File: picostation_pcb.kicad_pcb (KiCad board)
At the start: 2 copper layers, 54.5 x 83.1 mm, 70 parts, among them J1 USB_C_Receptacle_USB2.0, J2 +, J3 D, J4 C, J5 G, J6 Conn_01x20, SW1 BOOT, U1 LM78M05_TO252, U3 RP2040, U4 W25Q16JVSSIQ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

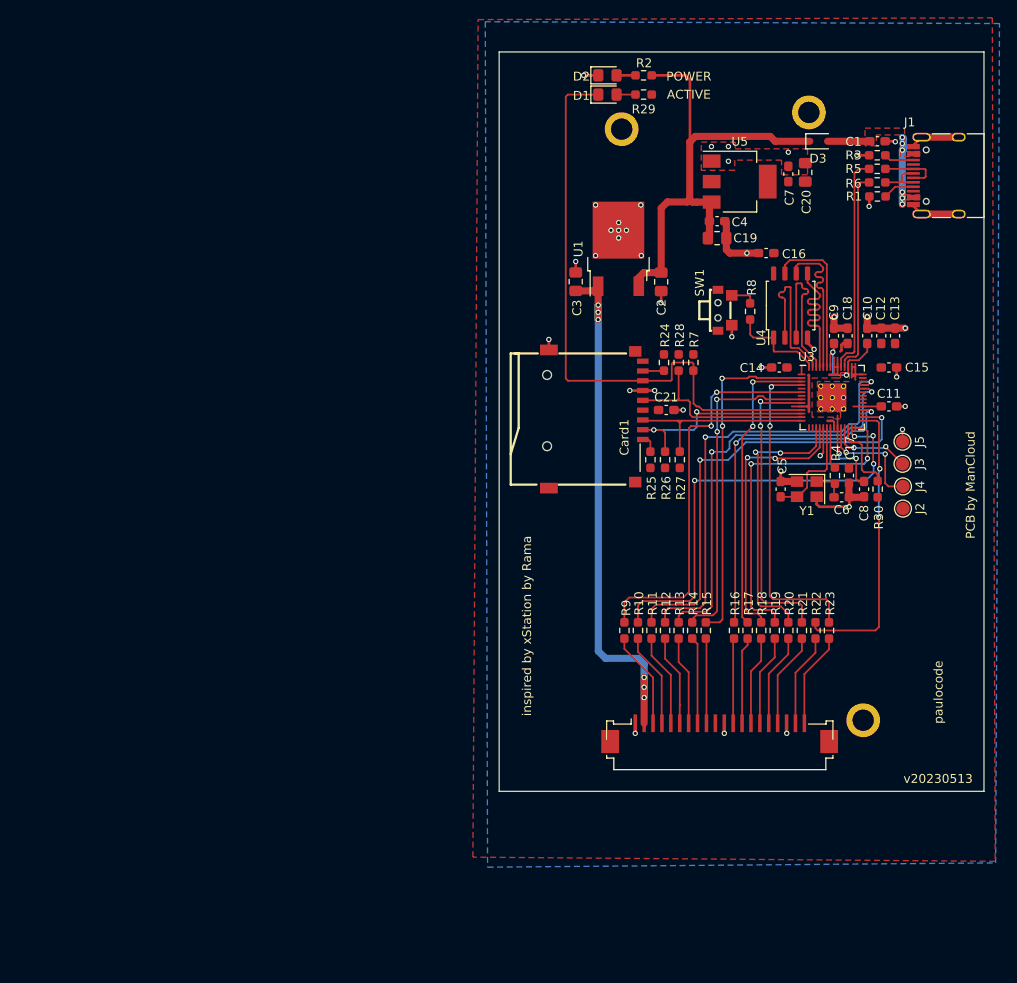
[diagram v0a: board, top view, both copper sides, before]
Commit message: Small PCB Improvements
Ordered a fully assembled board from JLCPCB, tested it for 5+ hours
while playing the fan translation of Policenauts. Tested several
other games as well for a short period of time (Silent Hill, Crash
Bandicoot, Spyro)

- Remove 5V 7805 regulator, diode OR the power from the 8V line into the
  AMS1117-3v3 instead (this part can accept up to 18V)
- Add a debug header that is compatible with the Raspberry Pi Debug
  Probe
- Add a reset switch
- Update photos
- Replace 2.2k resistors with 1k to improve ease of manufacturing
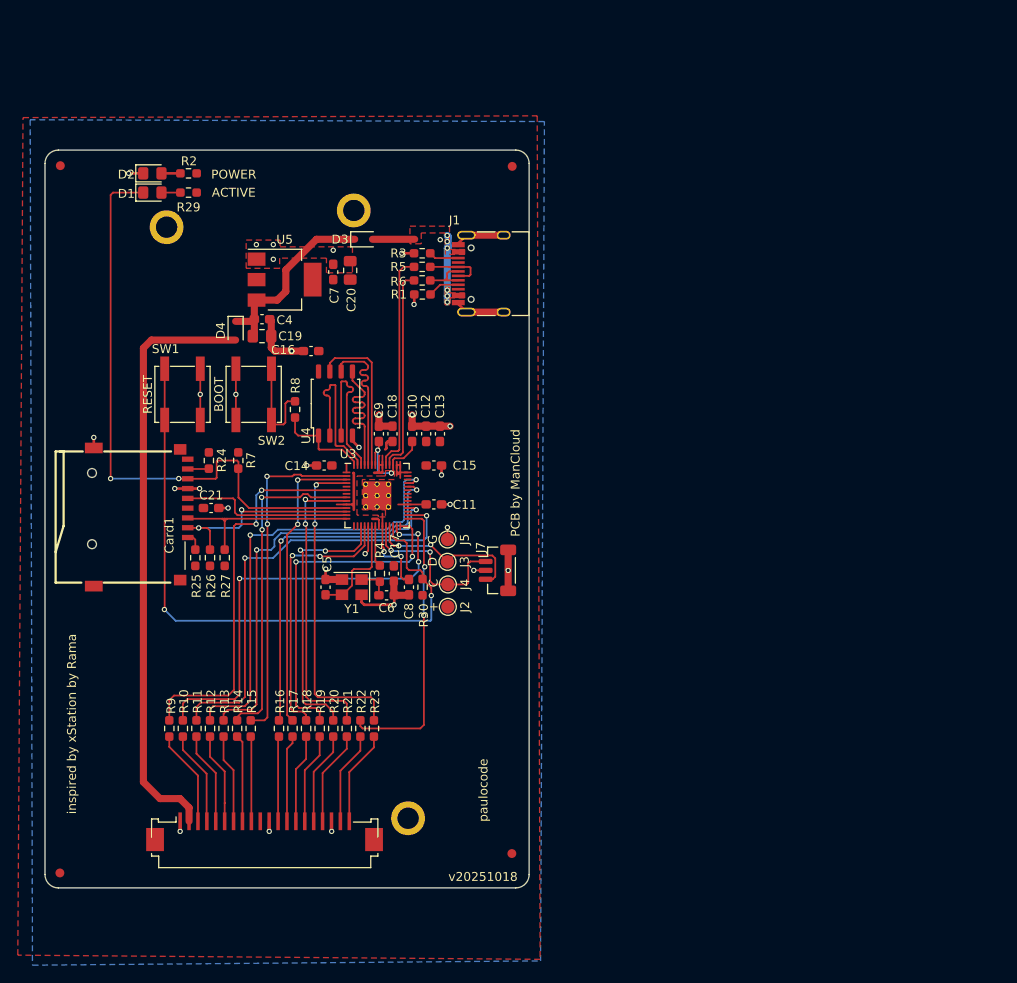
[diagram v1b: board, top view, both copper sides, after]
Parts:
- removed C1: 4.7u, Capacitor_SMD:C_0603_1608Metric_Pad1.08x0.95mm_HandSolder
- removed C2, C3: 10u, Capacitor_SMD:C_0805_2012Metric_Pad1.18x1.45mm_HandSolder
- removed R28: 10k, Resistor_SMD:R_0603_1608Metric_Pad0.98x0.95mm_HandSolder
- removed U1: LM78M05_TO252, Package_TO_SOT_SMD:TO-252-2
- added D4: 1N5819WS, Diode_SMD:D_SOD-323, F.Cu at (144.7, 75.0)
- added FID1: Fiducial, Fiducial:Fiducial_1mm_Mask2mm, F.Cu at (125.0, 56.5)
- added FID2: Fiducial, Fiducial:Fiducial_1mm_Mask2mm, F.Cu at (175.8, 56.6)
- added FID3: Fiducial, Fiducial:Fiducial_1mm_Mask2mm, F.Cu at (125.0, 136.0)
- added FID4: Fiducial, Fiducial:Fiducial_1mm_Mask2mm, F.Cu at (175.8, 133.8)
- added J7: SWD, Connector_JST:JST_SH_BM03B-SRSS-TB_1x03-1MP_P1.00mm_Vertical, F.Cu at (174.1, 102.0)
- added SW2: BOOT, Button_Switch_SMD:SW_SPST_EVPBF, F.Cu at (146.8, 82.2)
- H1, H2, H3: value MountingHole_Pad -> ~
- J1: value USB_C_Receptacle_USB2.0 -> USB_IN
- R2, R29: value 2.2k -> 1k
- SW1: value BOOT -> RESET; footprint kicad_lceda:SW-SMD_TS24CA -> Button_Switch_SMD:SW_SPST_EVPBF
- moved SW1 61.7 mm to (138.8, 82.2)
- moved J2 52.3 mm to (168.6, 106.1)
- moved C10 52.3 mm to (164.6, 86.6)
- moved C11 52.3 mm to (167.0, 94.6)
- moved C15 52.3 mm to (167.0, 90.2)
- moved C17 52.3 mm to (162.5, 102.3)
- moved C18 52.3 mm to (162.3, 86.6)
- moved C19 52.3 mm to (147.7, 75.7)
- moved C20 52.3 mm to (157.6, 68.3)
- moved C4 52.3 mm to (147.7, 73.7)
- moved C7 52.3 mm to (155.7, 68.4)
- moved H1 52.3 mm to (164.1, 129.8)
- moved J3 52.3 mm to (168.5, 101.0)
- moved R16 52.3 mm to (149.6, 119.7)
- moved R17 52.3 mm to (151.1, 119.7)
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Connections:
- C19 pad 1: +5V -> Net-(D3-K)
- C4 pad 1: +5V -> Net-(D3-K)
- D3 pad 1: +5V -> Net-(D3-K)
- R2 pad 1: +5V -> +3V3
- R30 pad 2: Net-(U3-RUN) -> Net-(SW1-A)
- R8 pad 2: Net-(R8-Pad2) -> Net-(SW2-B)
- SW1 pad 1: unconnected-(SW1-Pad1) -> Net-(SW1-A)
- SW1 pad 2: unconnected-(SW1-Pad2) -> GND
- U3 pad 26: Net-(U3-RUN) -> Net-(SW1-A)
- U5 pad 3: +5V -> Net-(D3-K)
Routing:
- net Net-(SW1-A): track 0.00 -> 71.2 mm, vias 0 -> 2
- net +5V: track 53.3 -> 0.00 mm
- net Net-(D3-K): track 0.00 -> 21.7 mm
- net GND: track 65.7 -> 78.1 mm, vias 39 -> 31
- net Net-(SW2-B): track 0.00 -> 10.4 mm
- net SWDIO: track 9.34 -> 18.4 mm
- net Net-(U3-RUN): track 8.57 -> 0.00 mm
- net SWCLK: track 12.8 -> 19.4 mm
- net +8V: track 61.6 -> 67.3 mm, vias 6 -> 0
- net SD_CLK: track 23.0 -> 19.4 mm
- net Net-(R8-Pad2): track 2.89 -> 0.00 mm
- net SD_MISO: track 68.7 -> 68.6 mm, vias 0 -> 2
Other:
- board size 54.5 x 83.1 mm -> 54.4 x 82.9 mm
- board text added: "v20251018"
- board text removed: "v20230513"
